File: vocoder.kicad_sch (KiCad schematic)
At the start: 36 parts, among them J1 AudioJack4, J2 Conn_01x02_Socket, J3 Conn_01x02_Pin, Q1 Q_NPN_BCE, Q2 Q_NPN_BCE, Q3 Q_NPN_BCE, Q4 Q_NPN_BCE, Q5 Q_NPN_BCE, SW1 SW_SPDT, SW2 SW_DIP_x05, U1 MAX4466EXK, U2 MAX98357A, U3 MT3608, U4 XIAO-ESP32-S3-SMD

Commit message: complete redesign of board and circuit, smaller and more powerful
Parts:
- removed D3: SS34, Diode_SMD:D_SMA, symbol Diode:SS34
- removed D4, D5, D6, D7, D8: 1N4148WS, Diode_SMD:D_SOD-323, symbol Diode:1N4148WS
- removed L1: 22u, Inductor_SMD:L_Neosid_SM-PIC0512H, symbol Device:L
- removed Q4, Q5: Q_NPN_BCE, Package_TO_SOT_SMD:SOT-23, symbol Transistor_BJT:Q_NPN_BCE
- removed R8: 15k, Resistor_SMD:R_0603_1608Metric_Pad0.98x0.95mm_HandSolder, symbol Device:R
- removed SW2: SW_DIP_x05, Button_Switch_SMD:SW_DIP_SPSTx05_Slide_6.7x14.26mm_W8.61mm_P2.54mm_LowProfile, symbol Switch:SW_DIP_x05
- removed U1: MAX4466EXK, MAX4466EXK:SOT65P210X110-5N, symbol MAX4466EXK:MAX4466EXK
- removed U2: MAX98357A, Package_DFN_QFN:TQFN-16-1EP_3x3mm_P0.5mm_EP1.23x1.23mm, symbol Audio:MAX98357A
- removed U3: MT3608, Package_TO_SOT_SMD:SOT-23-6, symbol Regulator_Switching:MT3608
- removed U4: XIAO-ESP32-S3-SMD, Seeed Studio XIAO Series Library:XIAO-ESP32S3-SMD, symbol Seeed_Studio_XIAO_Series:XIAO-ESP32-S3-SMD
- added C10, C11: 0.1u, Capacitor_SMD:C_0603_1608Metric, symbol Device:C
- added C13: 1u, Capacitor_SMD:C_0603_1608Metric, symbol Device:C
- added C3, C5, C6: 100n, Capacitor_SMD:C_0603_1608Metric, symbol Device:C
- added C4, C7, C8: 10u, Capacitor_SMD:C_0603_1608Metric, symbol Device:C
- added J4: USB_C_Receptacle_USB2.0_16P, Connector_USB:USB_C_Receptacle_GCT_USB4105-xx-A_16P_TopMnt_Horizontal, symbol Connector:USB_C_Receptacle_USB2.0_16P
- added SW2, SW3: SW_Push, Button_Switch_THT:SW_PUSH_1P1T_6x3.5mm_H5.0_APEM_MJTP1250, symbol Switch:SW_Push
- added U1: ESP32-S3-MINI-1, RF_Module:ESP32-S2-MINI-1, symbol RF_Module:ESP32-S3-MINI-1
- added U2: TP4056-42-ESOP8, Package_SO:SOIC-8-1EP_3.9x4.9mm_P1.27mm_EP2.41x3.3mm_ThermalVias, symbol Battery_Management:TP4056-42-ESOP8
- added U3: TPS73633DBV, Package_TO_SOT_SMD:SOT-23-5, symbol Regulator_Linear:TPS73633DBV
- added U5: ADAU1761, Package_CSP:LFCSP-32-1EP_5x5mm_P0.5mm_EP3.5x3.5mm_ThermalVias, symbol Audio:ADAU1761
- C1, C2: footprint Capacitor_SMD:C_0805_2012Metric -> Capacitor_SMD:C_0603_1608Metric
- R10, R9: value 100k -> 5.1k
- R3: value 160 -> 10k
- R4: value 160 -> 100k
- R5: value 140 -> 10k
- R6: value 1k -> 10k
- R7: value 110k -> 1.2k
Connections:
- net 3V3: now also C3.2, C4.2, C5.1, U5.1 (IOVDD), U5.23 (AVDD), U5.8 (AVDD)
- net 3V3_PRE: now also R5.1, R6.1, U1.3 (3V3), U3.5 (OUT)
- net 3V3_SWITCH: now also U1.9 (IO5)
- net BATT+: now also C2.2, U2.5 (BAT), U3.1 (IN), U3.3 (EN); no longer C2.1
- net BATT_READ: now also U1.10 (IO6)
- net BUZZER: now also U1.8 (IO4)
- net GND: now also C1.1, C2.1, J1.S, J3.1 (Pin_1), R10.2, R7.2, C10.2, C11.2, C13.1, C3.1, C4.1, C5.2, C6.1, C7.1, C8.1, J4.A1 (GND), J4.A12 (GND), J4.B1 (GND), J4.B12 (GND), J4.S1 (SHIELD), SW2.1, SW3.1, U1.1 (GND), U1.2 (GND), U1.42 (GND), U1.43 (GND), U1.46 (GND), U1.47 (GND), U1.48 (GND), U1.49 (GND), U1.50 (GND), U1.51 (GND), U1.52 (GND), U1.53 (GND), U1.54 (GND), U1.55 (GND), U1.56 (GND), U1.57 (GND), U1.58 (GND), U1.59 (GND), U1.60 (GND), U1.61 (GND), U1.62 (GND), U1.63 (GND), U1.64 (GND), U1.65 (GND), U2.1 (TEMP), U2.3 (GND), U2.6 (~{STDBY}), U2.7 (~{CHRG}), U2.9 (EPAD), U3.2 (GND), U5.22 (AGND), U5.25 (DGND), U5.3 (ADDR0/~{CLATCH}), U5.30 (ADDR1/CDATA), U5.33 (EP), U5.9 (AGND); no longer C1.2, C2.2, R6.2
- net I2S_BCLK: now also U1.37 (IO41), U5.28 (BCLK/GPIO2)
- net I2S_LRCLK: now also U1.36 (IO40), U5.29 (LRCLK/GPIO3)
- net LED_LEFT: now also U1.5 (IO1)
- net LED_RIGHT: now also U1.6 (IO2)
- net SWITCH_INPUT: now also U1.17 (IO13)
- net EN: now reaches R5.2
- net EN: now also C10.1, SW2.2, U1.45 (EN); no longer R6.1
- net at R10.1: now also J4.B5 (CC2)
- net at R9.1: now also J4.A5 (CC1)
- net at J1.R2: now also U5.10 (LINP), U5.12 (RINP)
- net at J3.2 (Pin_2): now also U5.21 (MONOOUT)
- removed net 5V: C1.1, R10.2, R5.1, R7.1
- new net: C13.2, U3.4 (NR)
- new net: R7.1, U2.2 (PROG)
- new net: C6.2, C7.2, U5.24 (DVDDOUT)
- new net: C8.2, U5.7 (CM)
- new net BOOT: C11.1, R6.2, SW3.2, U1.4 (IO0)
- new net I2S_DATA_IN: U1.30 (IO48), U5.27 (DAC_SDATA/GPIO0)
- new net I2S_DATA_OUT: U1.27 (IO47), U5.26 (ADC_SDATA/GPIO1)
- new net I2S_MCLK: U1.25 (IO21), U5.2 (MCLK)
- new net SCL: U1.16 (IO12), U5.32 (SCL/CCLK)
- new net SDA: U1.15 (IO11), U5.31 (SDA/COUT)
- new net USB+: J4.A6 (D+), J4.B6 (D+), U1.24 (USB_D+)
- new net USB-: J4.A7 (D-), J4.B7 (D-), U1.23 (USB_D-)
- new net USB_5V: C1.2, J4.A4 (VBUS), J4.A9 (VBUS), J4.B4 (VBUS), J4.B9 (VBUS), U2.4 (V_{CC}), U2.8 (CE)
- no-connect marks 13 -> 28
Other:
- moved on the sheet: J1, J3

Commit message: fixed minor error
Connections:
- no-connect marks 28 -> 40
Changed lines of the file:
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@@
+	)
+	(no_connect
+		(at 66.04 76.2)
 	)
 	(no_connect
@@
 	)
 	(no_connect
+		(at 96.52 33.02)
+	)
+	(no_connect
 		(at 53.34 173.99)
 	)
 	(no_connect
+		(at 66.04 53.34)
+	)
+	(no_connect
+		(at 66.04 58.42)
+	)
+	(no_connect
 		(at 215.9 69.85)
+	)
+	(no_connect
+		(at 96.52 71.12)
+	)
+	(no_connect
+		(at 66.04 73.66)
 	)
 	(no_connect
@@
 	)
 	(no_connect
+		(at 96.52 30.48)
+	)
+	(no_connect
 		(at 215.9 62.23)
+	)
+	(no_connect
+		(at 66.04 71.12)
 	)
 	(no_connect
@@
 	)
 	(no_connect
+		(at 66.04 78.74)
+	)
+	(no_connect
 		(at 215.9 39.37)
 	)
@@
 	(no_connect
 		(at 96.52 53.34)
+	)
+	(no_connect
+		(at 66.04 55.88)
 	)
 	(no_connect
@@
 	)
 	(no_connect
+		(at 66.04 81.28)
+	)
+	(no_connect
 		(at 96.52 76.2)
 	)
 	(no_connect
+		(at 66.04 60.96)
+	)
+	(no_connect

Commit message: changed buttons to smaller SMT ones
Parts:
- SW2, SW3: footprint Button_Switch_THT:SW_PUSH_1P1T_6x3.5mm_H5.0_APEM_MJTP1250 -> Button_Switch_SMD:SW_Push_SPST_NO_Alps_SKRK
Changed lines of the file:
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@@
 			)
 		)
-		(property "Footprint" "Button_Switch_THT:SW_PUSH_1P1T_6x3.5mm_H5.0_APEM_MJTP1250"
+		(property "Footprint" "Button_Switch_SMD:SW_Push_SPST_NO_Alps_SKRK"
 			(at 19.05 43.18 0)
 			(effects
@@
 			)
 		)
-		(property "Footprint" "Button_Switch_THT:SW_PUSH_1P1T_6x3.5mm_H5.0_APEM_MJTP1250"
+		(property "Footprint" "Button_Switch_SMD:SW_Push_SPST_NO_Alps_SKRK"
 			(at 19.05 20.32 0)
 			(effects

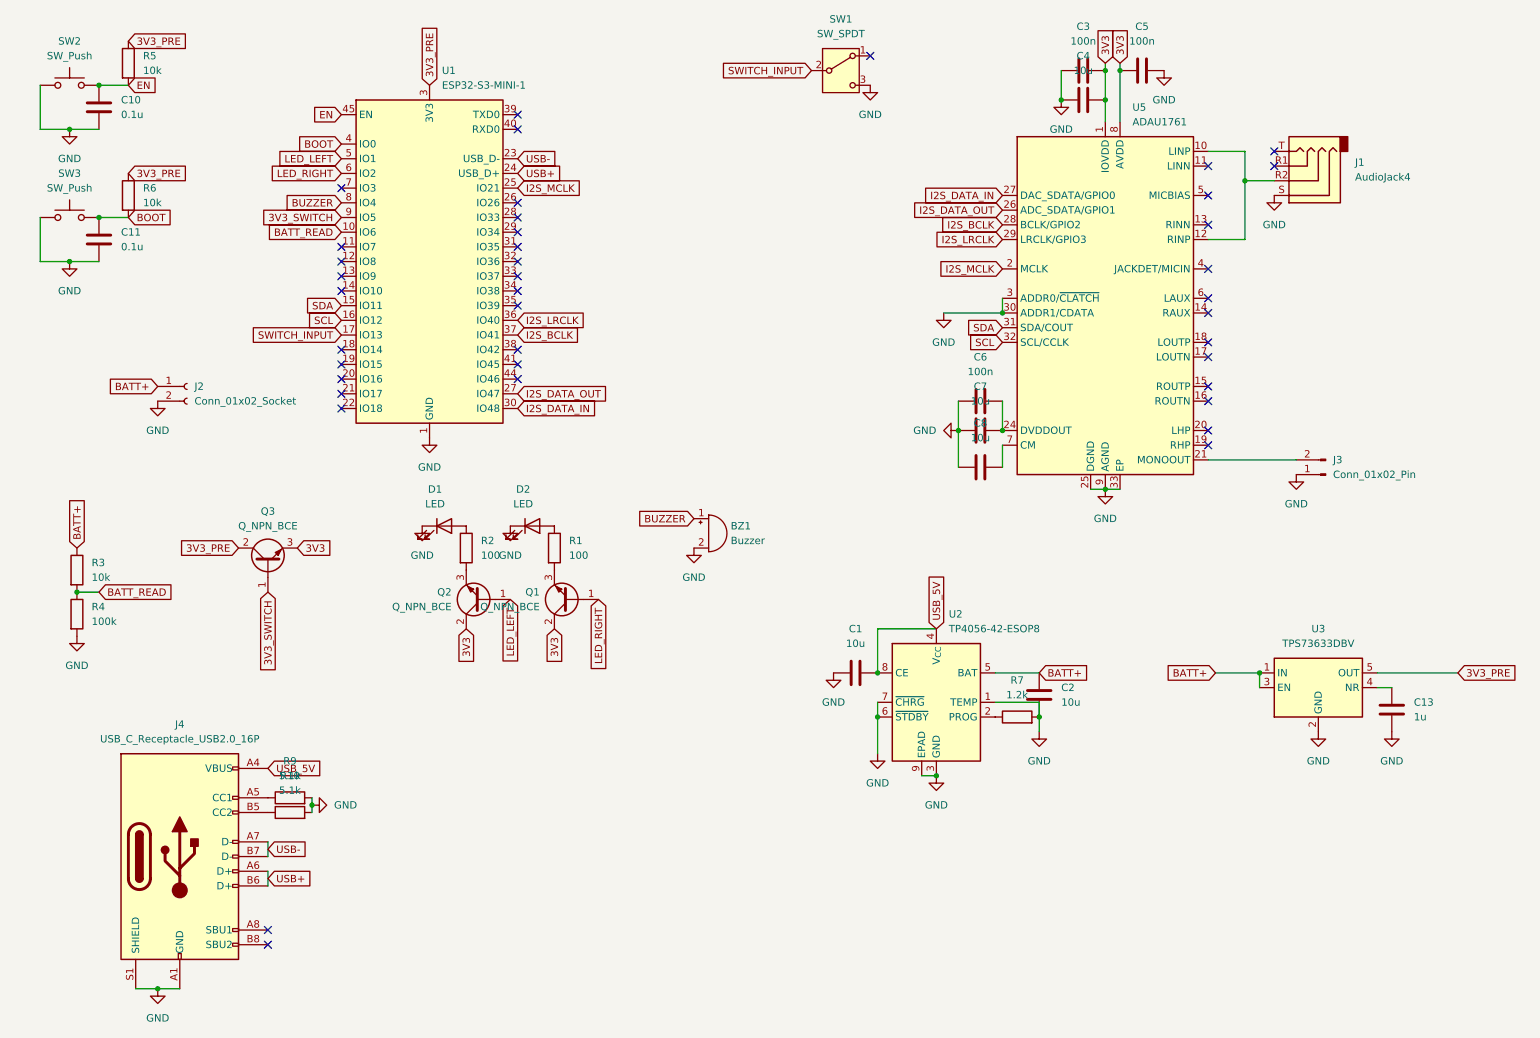
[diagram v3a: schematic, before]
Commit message: added debug led's
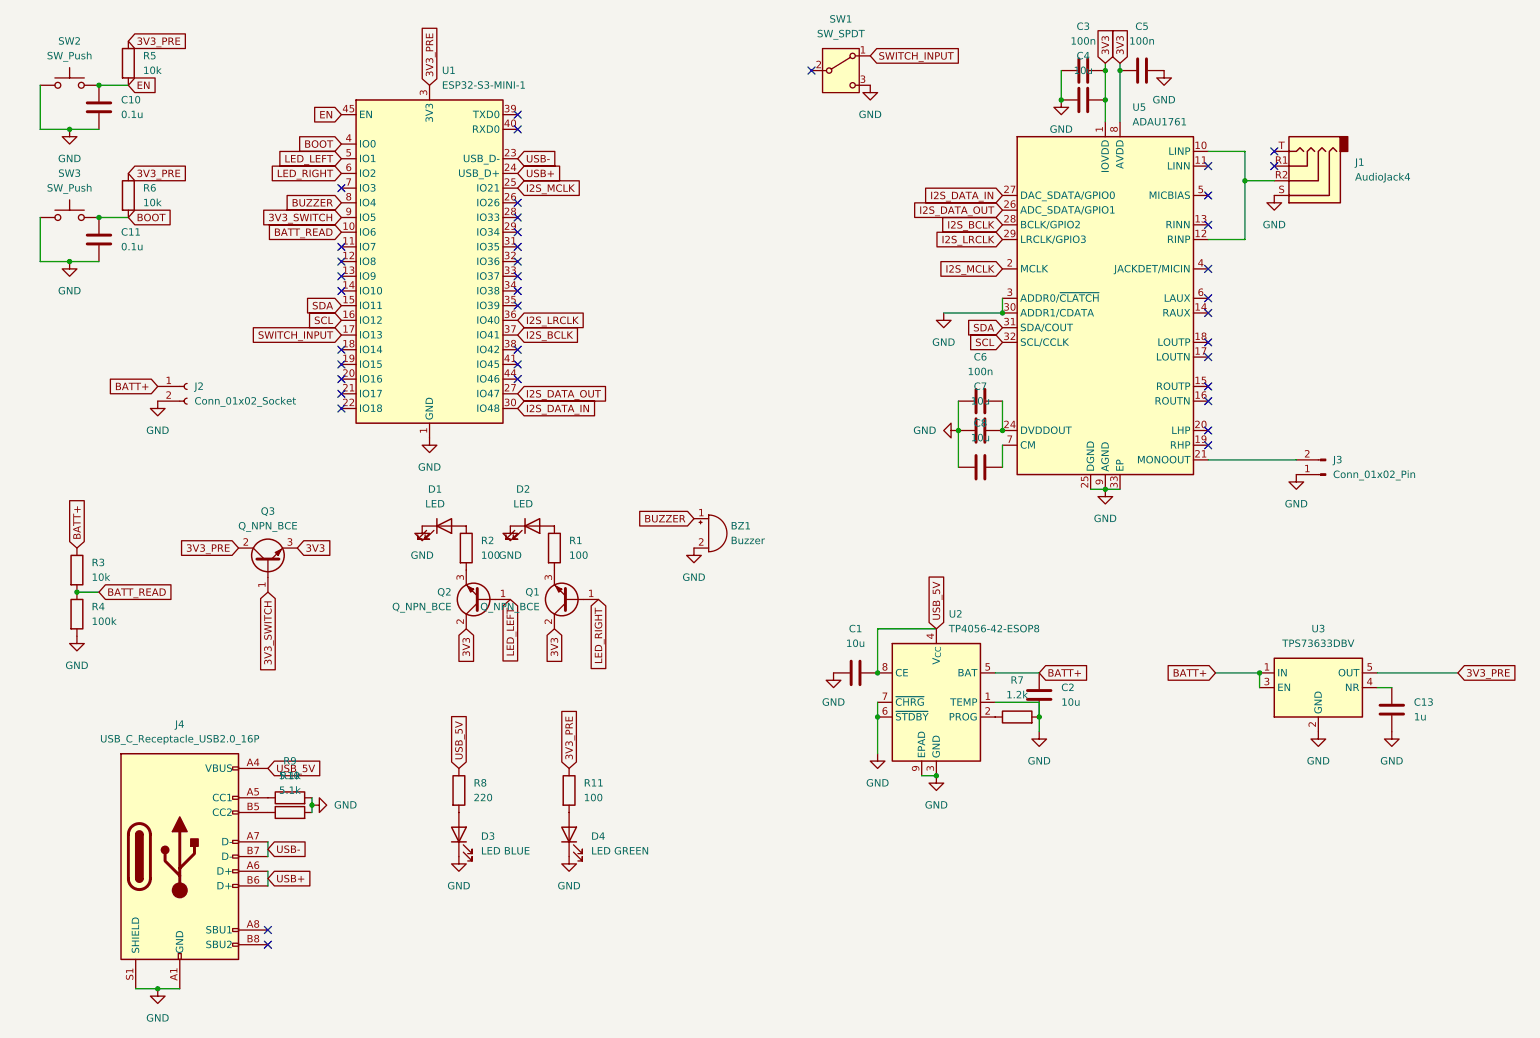
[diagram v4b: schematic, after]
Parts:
- added D3: LED BLUE, LED_SMD:LED_0603_1608Metric, symbol Device:LED
- added D4: LED GREEN, LED_SMD:LED_0603_1608Metric, symbol Device:LED
- added R11: 100, Resistor_SMD:R_0603_1608Metric_Pad0.98x0.95mm_HandSolder, symbol Device:R
- added R8: 220, Resistor_SMD:R_0603_1608Metric_Pad0.98x0.95mm_HandSolder, symbol Device:R
- D1, D2: footprint LED_SMD:LED_1206_3216Metric_Pad1.42x1.75mm_HandSolder -> LED_SMD:LED_0603_1608Metric
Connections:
- net 3V3_PRE: now also R11.1
- net GND: now also D3.1 (K), D4.1 (K)
- net SWITCH_INPUT: now also SW1.1 (A); no longer SW1.2 (B)
- net USB_5V: now also R8.1
- new net: D3.2 (A), R8.2
- new net: D4.2 (A), R11.2
